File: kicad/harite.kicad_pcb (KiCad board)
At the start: 2 copper layers, 258.2 x 95.8 mm, 80 parts, among them J1 503480-0500, J2 Wired Joystick, J4 5034801200, J5 5034801200, U1 RP2040_Zero, U2 RP2040_Zero

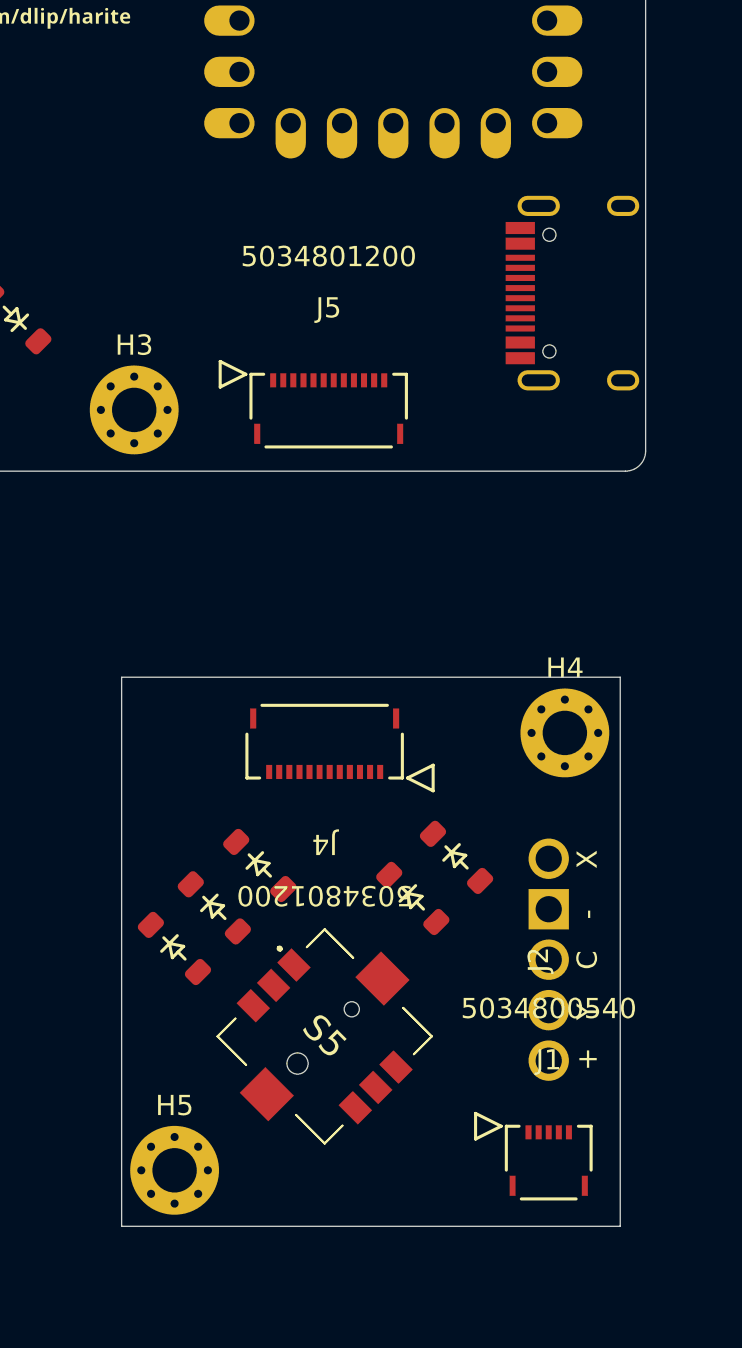
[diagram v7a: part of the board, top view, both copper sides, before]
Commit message: move diodes
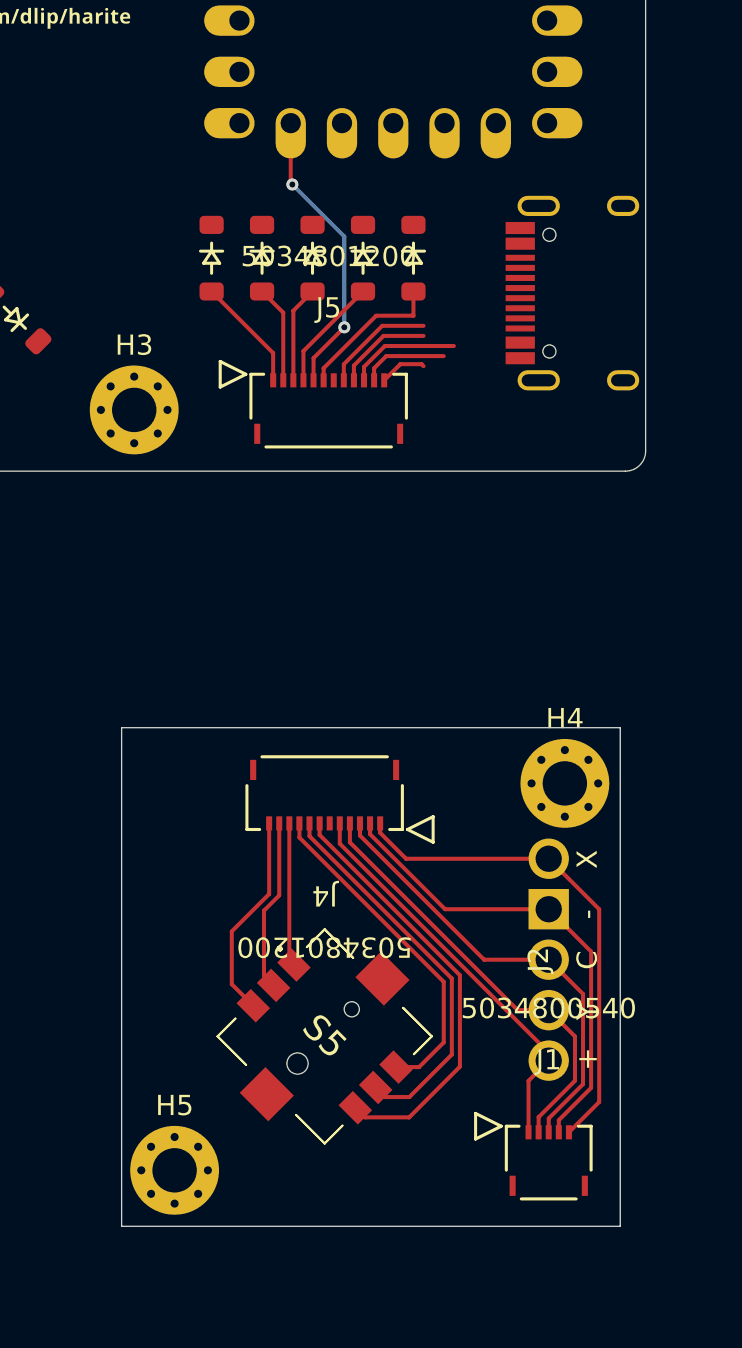
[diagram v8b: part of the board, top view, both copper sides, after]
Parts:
- moved D23 34.2 mm to (124.0, 89.7), turned to -90 degrees
- moved D22 32.3 mm to (126.5, 89.7), turned to -90 degrees
- moved D24 31.8 mm to (131.5, 89.7), turned to -90 degrees
- moved D21 30.2 mm to (129.0, 89.7), turned to -90 degrees
- moved D25 29.8 mm to (134.0, 89.7), turned to -90 degrees
- moved J4 2.55 mm to (129.6, 116.2)
- moved H4 2.50 mm to (141.5, 115.7)
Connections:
- D21 pad 1: ERow 1 -> Row 1
- D22 pad 1: ERow 2 -> Row 2
- D23 pad 1: ERow 3 -> Row 3
- D24 pad 1: ERow 4 -> Row 4
- D25 pad 1: ERow 5 -> Row 5
- J4 pad 1: ECol 5 -> EJX
- J4 pad 10: EJC -> ERow 1
- J4 pad 11: EJY -> ERow 2
- J4 pad 12: E3V3 -> ERow 3
- J4 pad 2: ERow 5 -> EGND
- J4 pad 3: ERow 4 -> EJC
- J4 pad 4: ERow 3 -> EJY
- J4 pad 5: ERow 2 -> E3V3
- J4 pad 6: ERow 1 -> unconnected-(J4-Pad6)
- J4 pad 7: unconnected-(J4-Pad7) -> ERow 5
- J4 pad 8: EJX -> ECol 5
- J4 pad 9: EGND -> ERow 4
- J5 pad 1: 3V3 -> Net-(D23-A)
- J5 pad 10: Row 4 -> JC
- J5 pad 11: Row 5 -> GND
- J5 pad 12: Col 5 -> JX
- J5 pad 2: JY -> Net-(D22-A)
- J5 pad 3: JC -> Net-(D21-A)
- J5 pad 4: GND -> Net-(D24-A)
- J5 pad 5: JX -> Col 5
- J5 pad 6: unconnected-(J5-Pad6) -> Net-(D25-A)
- J5 pad 7: Row 1 -> unconnected-(J5-Pad7)
- J5 pad 8: Row 2 -> 3V3
- J5 pad 9: Row 3 -> JY
- S5 pad 1: Net-(D21-A) -> ERow 1
- S5 pad 2: Net-(D22-A) -> ERow 2
- S5 pad 3: Net-(D23-A) -> ERow 3
- S5 pad 4: Net-(D24-A) -> ERow 4
- S5 pad 6: Net-(D25-A) -> ERow 5
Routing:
- net EJX: track 0.00 -> 24.6 mm
- net EGND: track 0.00 -> 23.5 mm
- net EJC: track 0.00 -> 22.5 mm
- net EJY: track 0.00 -> 21.6 mm
- net ERow 5: track 0.00 -> 21.3 mm
- net E3V3: track 0.00 -> 20.0 mm
- net ECol 5: track 0.00 -> 19.2 mm
- net ERow 4: track 0.00 -> 16.7 mm
- net Col 5: track 0.00 -> 14.5 mm, vias 0 -> 2
- net ERow 3: track 0.00 -> 10.2 mm
- net ERow 2: track 0.00 -> 8.53 mm
- net Net-(D25-A): track 0.00 -> 7.33 mm
- net ERow 1: track 0.00 -> 7.11 mm
- net Net-(D23-A): track 0.00 -> 5.66 mm
- net Net-(D24-A): track 0.00 -> 5.62 mm
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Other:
- outline, holes or cut-outs redrawn
